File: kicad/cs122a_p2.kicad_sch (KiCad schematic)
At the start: 12 parts, among them U1 STM32F042K6Tx, U2 Digit 1, U3 Digit 2, U4 Digit 3, U5 SN7447A

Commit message: Added footprints to all current parts
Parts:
- R1, R2, R3, R4, R5, R6, R7: footprint (none) -> Resistor_THT:R_Axial_DIN0204_L3.6mm_D1.6mm_P7.62mm_Horizontal
- U2, U3, U4: footprint (none) -> cs122a_p2:3161BS
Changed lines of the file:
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@@
       (effects (font (size 1.27 1.27)))
     )
-    (property "Footprint" "" (at 261.62 38.1 0)
+    (property "Footprint" "cs122a_p2:3161BS" (at 261.62 38.1 0)
       (effects (font (size 1.27 1.27)) hide)
     )
@@
       (effects (font (size 1.27 1.27)))
     )
-    (property "Footprint" "" (at 232.664 42.164 90)
+    (property "Footprint" "Resistor_THT:R_Axial_DIN0204_L3.6mm_D1.6mm_P7.62mm_Horizontal" (at 232.664 42.164 90)
       (effects (font (size 1.27 1.27)) hide)
     )
@@
       (effects (font (size 1.27 1.27)))
     )
-    (property "Footprint" "" (at 232.664 68.834 90)
+    (property "Footprint" "Resistor_THT:R_Axial_DIN0204_L3.6mm_D1.6mm_P7.62mm_Horizontal" (at 232.664 68.834 90)
       (effects (font (size 1.27 1.27)) hide)
     )
@@
       (effects (font (size 1.27 1.27)))
     )
-    (property "Footprint" "" (at 261.62 59.69 0)
+    (property "Footprint" "cs122a_p2:3161BS" (at 261.62 59.69 0)
       (effects (font (size 1.27 1.27)) hide)
     )
@@
       (effects (font (size 1.27 1.27)))
     )
-    (property "Footprint" "" (at 232.664 77.724 90)
+    (property "Footprint" "Resistor_THT:R_Axial_DIN0204_L3.6mm_D1.6mm_P7.62mm_Horizontal" (at 232.664 77.724 90)
       (effects (font (size 1.27 1.27)) hide)
     )
@@
       (effects (font (size 1.27 1.27)))
     )
-    (property "Footprint" "" (at 232.664 33.274 90)
+    (property "Footprint" "Resistor_THT:R_Axial_DIN0204_L3.6mm_D1.6mm_P7.62mm_Horizontal" (at 232.664 33.274 90)
       (effects (font (size 1.27 1.27)) hide)
     )
@@
       (effects (font (size 1.27 1.27)))
     )
-    (property "Footprint" "" (at 232.664 59.944 90)
+    (property "Footprint" "Resistor_THT:R_Axial_DIN0204_L3.6mm_D1.6mm_P7.62mm_Horizontal" (at 232.664 59.944 90)
       (effects (font (size 1.27 1.27)) hide)
     )
@@
       (effects (font (size 1.27 1.27)))
     )
-    (property "Footprint" "" (at 261.62 80.01 0)
+    (property "Footprint" "cs122a_p2:3161BS" (at 261.62 80.01 0)
       (effects (font (size 1.27 1.27)) hide)
     )
@@
       (effects (font (size 1.27 1.27)))
     )
-    (property "Footprint" "" (at 232.664 24.384 90)
+    (property "Footprint" "Resistor_THT:R_Axial_DIN0204_L3.6mm_D1.6mm_P7.62mm_Horizontal" (at 232.664 24.384 90)
       (effects (font (size 1.27 1.27)) hide)
     )
@@
       (effects (font (size 1.27 1.27)))
     )
-    (property "Footprint" "" (at 232.664 51.054 90)
-      (effects (font (size 1.27 1.27)) hide)
-    )
+    (property "Footprint" "Resistor_THT:R_Axial_DIN0204_L3.6mm_D1.6mm_P7.62mm_Horizontal" (at 232.664 51.054 90)
+      (effects (font (size 1.27 1.27)) hide)
+    )

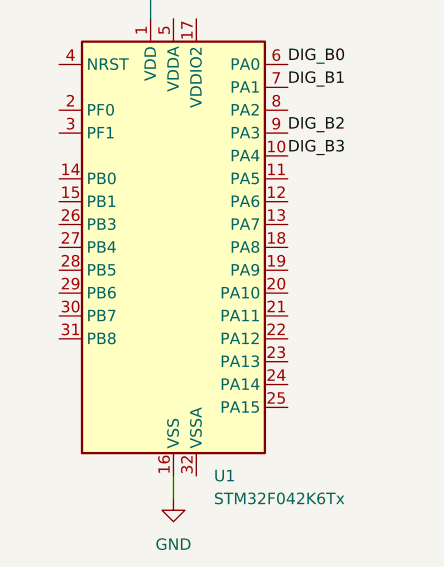
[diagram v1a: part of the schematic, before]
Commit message: Updated enable connections to match 7934d89
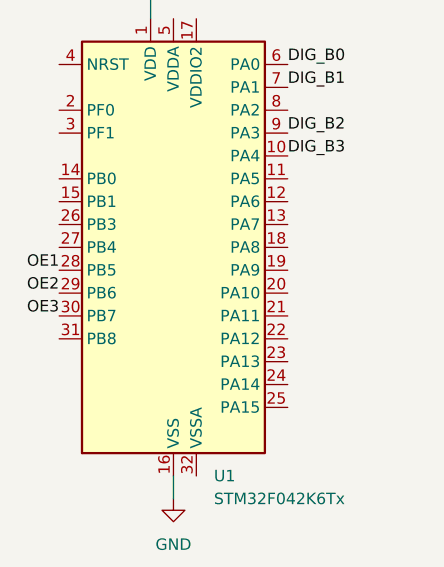
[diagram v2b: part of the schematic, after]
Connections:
- net OE1: now also U1.28 (PB5)
- net OE2: now also U1.29 (PB6)
- net OE3: now also U1.30 (PB7)
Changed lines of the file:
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@@
+    (effects (font (size 1.27 1.27)) (justify right bottom))
+  )
+  (label "OE1" (at 123.19 106.68 180) (fields_autoplaced)
     (effects (font (size 1.27 1.27)) (justify right bottom))
   )
@@
   (label "SEG_A" (at 270.51 57.15 0) (fields_autoplaced)
     (effects (font (size 1.27 1.27)) (justify left bottom))
+  )
+  (label "OE2" (at 123.19 109.22 180) (fields_autoplaced)
+    (effects (font (size 1.27 1.27)) (justify right bottom))
   )
   (label "DIG_B2" (at 193.04 49.53 180) (fields_autoplaced)
@@
     (effects (font (size 1.27 1.27)) (justify right bottom))
   )
+  (label "OE3" (at 123.19 111.76 180) (fields_autoplaced)
+    (effects (font (size 1.27 1.27)) (justify right bottom))
+  )

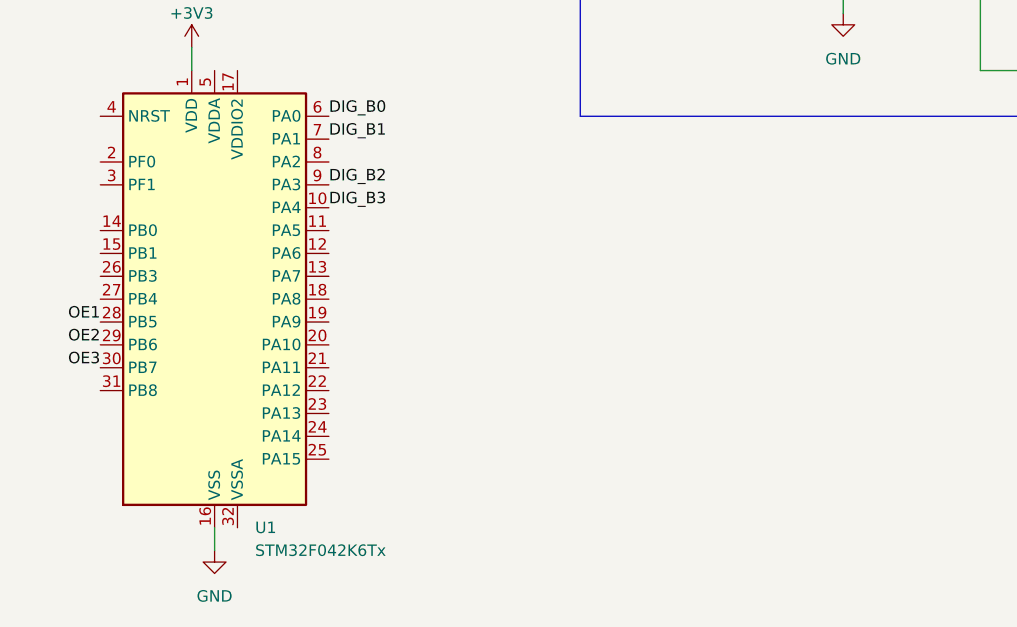
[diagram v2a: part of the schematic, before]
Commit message: Updated schematic to include tap, inc, and dec buttons
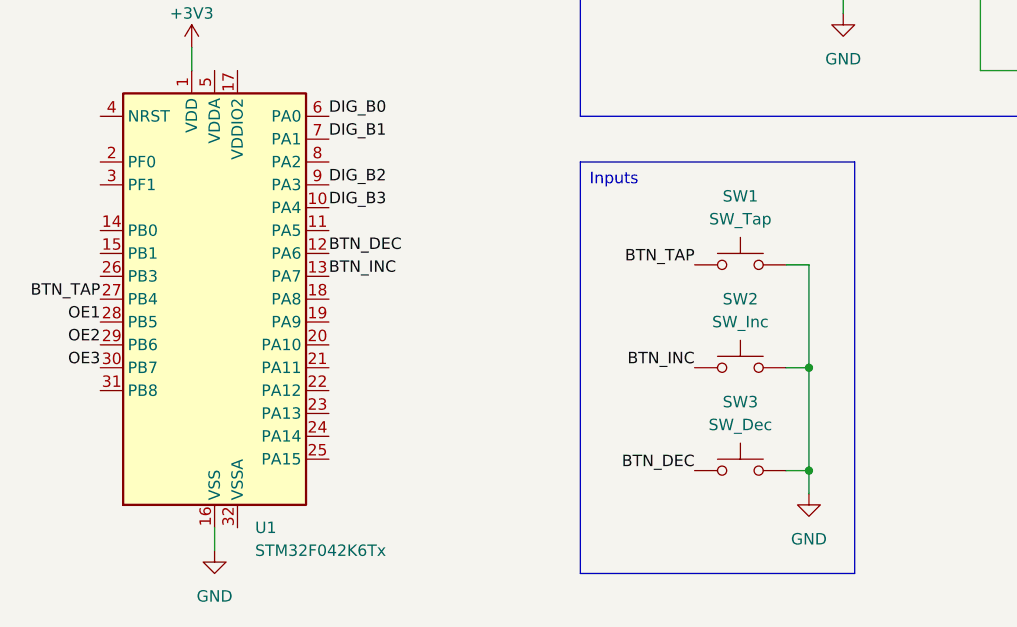
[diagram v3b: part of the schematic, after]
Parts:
- added SW1: SW_Tap, symbol Switch:SW_Push
- added SW2: SW_Inc, symbol Switch:SW_Push
- added SW3: SW_Dec, symbol Switch:SW_Push
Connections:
- net GND: now also SW1.2, SW2.2, SW3.2
- net BTN_DEC: now reaches U1.12 (PA6)
- net BTN_DEC: now also SW3.1
- net BTN_INC: now reaches U1.13 (PA7)
- net BTN_INC: now also SW2.1
- net BTN_TAP: now reaches U1.27 (PB4)
- net BTN_TAP: now also SW1.1
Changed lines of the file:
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@@
 (kicad_sch (version 20230121) (generator eeschema)
   (paper "A4")
+  (junction (at 201.93 111.76) (diameter 0) (color 0 0 0 0)
+  )
   (junction (at 181.61 59.69) (diameter 0) (color 0 0 0 0)
+  )
+  (junction (at 201.93 123.19) (diameter 0) (color 0 0 0 0)
   )
   (junction (at 181.61 57.15) (diameter 0) (color 0 0 0 0)
@@
     (stroke (width 0) (type default))
   )
+  (wire (pts (xy 199.39 111.76) (xy 201.93 111.76))
+    (stroke (width 0) (type default))
+  )
+  (wire (pts (xy 201.93 125.73) (xy 201.93 123.19))
+    (stroke (width 0) (type default))
+  )
   (wire (pts (xy 226.06 49.53) (xy 226.06 43.18))
     (stroke (width 0) (type default))
@@
     (stroke (width 0) (type default))
   )
+  (wire (pts (xy 201.93 111.76) (xy 201.93 123.19))
+    (stroke (width 0) (type default))
+  )
   (wire (pts (xy 228.6 34.29) (xy 223.52 34.29))
     (stroke (width 0) (type default))
@@
     (stroke (width 0) (type default))
   )
+  (wire (pts (xy 199.39 100.33) (xy 201.93 100.33))
+    (stroke (width 0) (type default))
+  )
   (wire (pts (xy 226.06 43.18) (xy 228.6 43.18))
     (stroke (width 0) (type default))
@@
     (stroke (width 0) (type default))
   )
+  (wire (pts (xy 201.93 100.33) (xy 201.93 111.76))
+    (stroke (width 0) (type default))
+  )
   (wire (pts (xy 226.06 54.61) (xy 226.06 60.96))
     (stroke (width 0) (type default))
@@
   )
   (wire (pts (xy 218.44 44.45) (xy 220.98 44.45))
+    (stroke (width 0) (type default))
+  )
+  (wire (pts (xy 201.93 123.19) (xy 199.39 123.19))
     (stroke (width 0) (type default))
   )
@@
     (effects (font (size 1.27 1.27)) (justify left top))
   )
+  (text_box "Inputs"
+    (at 176.53 88.9 0) (size 30.48 45.72)
+    (stroke (width 0) (type default))
+    (fill (type none))
+    (effects (font (size 1.27 1.27)) (justify left top))
+  )
   (label "SEG_D" (at 252.73 57.15 180) (fields_autoplaced)
     (effects (font (size 1.27 1.27)) (justify right bottom))
   )
+  (label "BTN_TAP" (at 189.23 100.33 180) (fields_autoplaced)
+    (effects (font (size 1.27 1.27)) (justify right bottom))
+  )
   (label "OE1" (at 123.19 106.68 180) (fields_autoplaced)
     (effects (font (size 1.27 1.27)) (justify right bottom))
   )
+  (label "BTN_TAP" (at 123.19 104.14 180) (fields_autoplaced)
+    (effects (font (size 1.27 1.27)) (justify right bottom))
+  )
   (label "SEG_A" (at 270.51 77.47 0) (fields_autoplaced)
     (effects (font (size 1.27 1.27)) (justify left bottom))
@@
     (effects (font (size 1.27 1.27)) (justify left bottom))
   )
+  (label "BTN_INC" (at 189.23 111.76 180) (fields_autoplaced)
+    (effects (font (size 1.27 1.27)) (justify right bottom))
+  )
   (label "DIG_B0" (at 148.59 83.82 0) (fields_autoplaced)
     (effects (font (size 1.27 1.27)) (justify left bottom))
@@
   )
   (label "SEG_G" (at 236.22 78.74 0) (fields_autoplaced)
+    (effects (font (size 1.27 1.27)) (justify left bottom))
+  )
+  (label "BTN_DEC" (at 148.59 99.06 0) (fields_autoplaced)
+    (effects (font (size 1.27 1.27)) (justify left bottom))
+  )
+  (label "BTN_DEC" (at 189.23 123.19 180) (fields_autoplaced)
+    (effects (font (size 1.27 1.27)) (justify right bottom))
+  )
+  (label "BTN_INC" (at 148.59 101.6 0) (fields_autoplaced)
     (effects (font (size 1.27 1.27)) (justify left bottom))
   )
@@
     )
   )
+  (symbol (lib_id "power:GND") (at 201.93 125.73 0) (unit 1)
+    (in_bom yes) (on_board yes) (dnp no) (fields_autoplaced)
+    (property "Reference" "#PWR06" (at 201.93 132.08 0)
+      (effects (font (size 1.27 1.27)) hide)
+    )
+    (property "Value" "GND" (at 201.93 130.81 0)
+      (effects (font (size 1.27 1.27)))
+    )
+    (property "Footprint" "" (at 201.93 125.73 0)
+      (effects (font (size 1.27 1.27)) hide)
+    )
+    (property "Datasheet" "" (at 201.93 125.73 0)
+      (effects (font (size 1.27 1.27)) hide)
+    )
+    (pin "1")
+    (instances
+      (project "cs122a_p2"
+        (path "/f5250a06-5d3f-42a4-81bc-c043e883a187"
+          (reference "#PWR06") (unit 1)
+        )
+      )
+    )
+  )
   (symbol (lib_id "Device:R_US") (at 232.41 60.96 90) (unit 1)
     (in_bom yes) (on_board yes) (dnp no)
@@
         (path "/f5250a06-5d3f-42a4-81bc-c043e883a187"
           (reference "R5") (unit 1)
+        )
+      )
+    )
+  )
+  (symbol (lib_id "Switch:SW_Push") (at 194.31 111.76 0) (unit 1)
+    (in_bom yes) (on_board yes) (dnp no) (fields_autoplaced)
+    (property "Reference" "SW2" (at 194.31 104.14 0)
+      (effects (font (size 1.27 1.27)))
+    )
+    (property "Value" "SW_Inc" (at 194.31 106.68 0)
+      (effects (font (size 1.27 1.27)))
+    )
+    (property "Footprint" "" (at 194.31 106.68 0)
+      (effects (font (size 1.27 1.27)) hide)
+    )
+    (property "Datasheet" "~" (at 194.31 106.68 0)
+      (effects (font (size 1.27 1.27)) hide)
+    )
+    (pin "1")
+    (pin "2")
+    (instances
+      (project "cs122a_p2"
+        (path "/f5250a06-5d3f-42a4-81bc-c043e883a187"
+          (reference "SW2") (unit 1)
         )
       )
@@
         )
       )
+    )
+  )
+  (symbol (lib_id "Switch:SW_Push") (at 194.31 123.19 0) (unit 1)
+    (in_bom yes) (on_board yes) (dnp no) (fields_autoplaced)
+    (property "Reference" "SW3" (at 194.31 115.57 0)
+      (effects (font (size 1.27 1.27)))
+    )
+    (property "Value" "SW_Dec" (at 194.31 118.11 0)
+      (effects (font (size 1.27 1.27)))
+    )
+    (property "Footprint" "" (at 194.31 118.11 0)
+      (effects (font (size 1.27 1.27)) hide)
+    )
+    (property "Datasheet" "~" (at 194.31 118.11 0)
+      (effects (font (size 1.27 1.27)) hide)
+    )
+    (pin "1")
+    (pin "2")
+    (instances
+      (project "cs122a_p2"
+        (path "/f5250a06-5d3f-42a4-81bc-c043e883a187"
+          (reference "SW3") (unit 1)
+        )
+      )
+    )
+  )
+  (symbol (lib_id "Switch:SW_Push") (at 194.31 100.33 0) (unit 1)
+    (in_bom yes) (on_board yes) (dnp no) (fields_autoplaced)
+    (property "Reference" "SW1" (at 194.31 92.71 0)
+      (effects (font (size 1.27 1.27)))
+    )
+    (property "Value" "SW_Tap" (at 194.31 95.25 0)
+      (effects (font (size 1.27 1.27)))
+    )
+    (property "Footprint" "" (at 194.31 95.25 0)
+      (effects (font (size 1.27 1.27)) hide)
+    )
+    (property "Datasheet" "~" (at 194.31 95.25 0)
+      (effects (font (size 1.27 1.27)) hide)
+    )
+    (pin "1")
+    (pin "2")
+    (instances
+      (project "cs122a_p2"
+        (path "/f5250a06-5d3f-42a4-81bc-c043e883a187"
+          (reference "SW1") (unit 1)
+        )
+      )

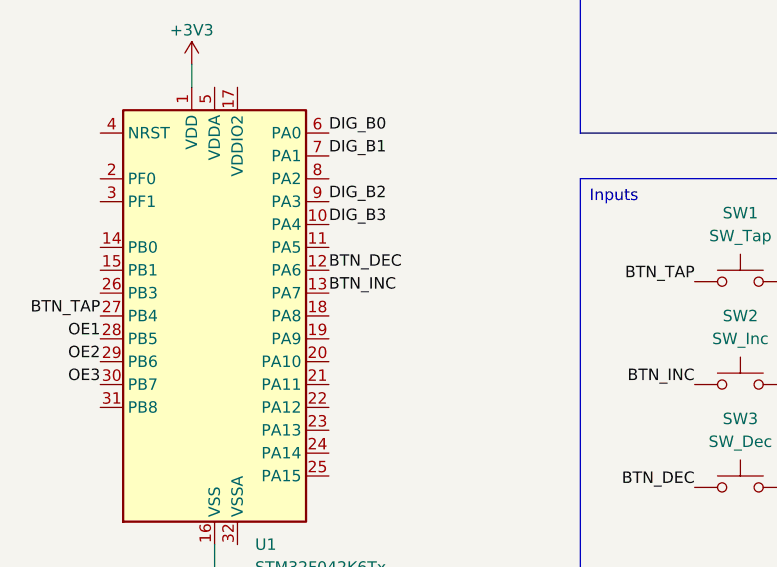
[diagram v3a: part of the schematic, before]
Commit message: Double and half button functionality
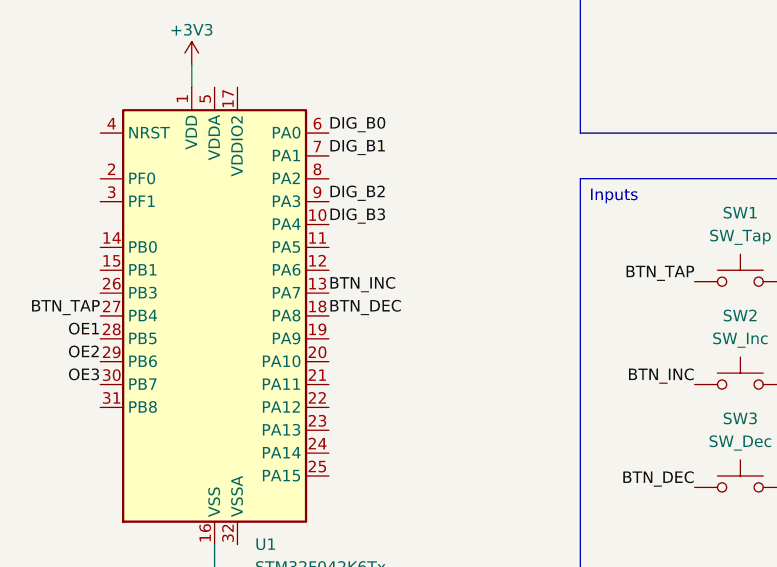
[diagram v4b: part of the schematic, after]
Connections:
- net BTN_DEC: now also U1.18 (PA8); no longer U1.12 (PA6)
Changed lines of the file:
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@@
     (effects (font (size 1.27 1.27)) (justify left top))
+  )
+  (label "BTN_DEC" (at 148.59 104.14 0) (fields_autoplaced)
+    (effects (font (size 1.27 1.27)) (justify left bottom))
   )
   (label "SEG_D" (at 252.73 57.15 180) (fields_autoplaced)
@@
     (effects (font (size 1.27 1.27)) (justify left bottom))
   )
-  (label "BTN_DEC" (at 148.59 99.06 0) (fields_autoplaced)
-    (effects (font (size 1.27 1.27)) (justify left bottom))
-  )
